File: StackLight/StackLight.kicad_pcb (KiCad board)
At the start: 2 copper layers, 40.6 x 35.5 mm, 3 parts, among them J1 RJ45, J2 Conn_01x05

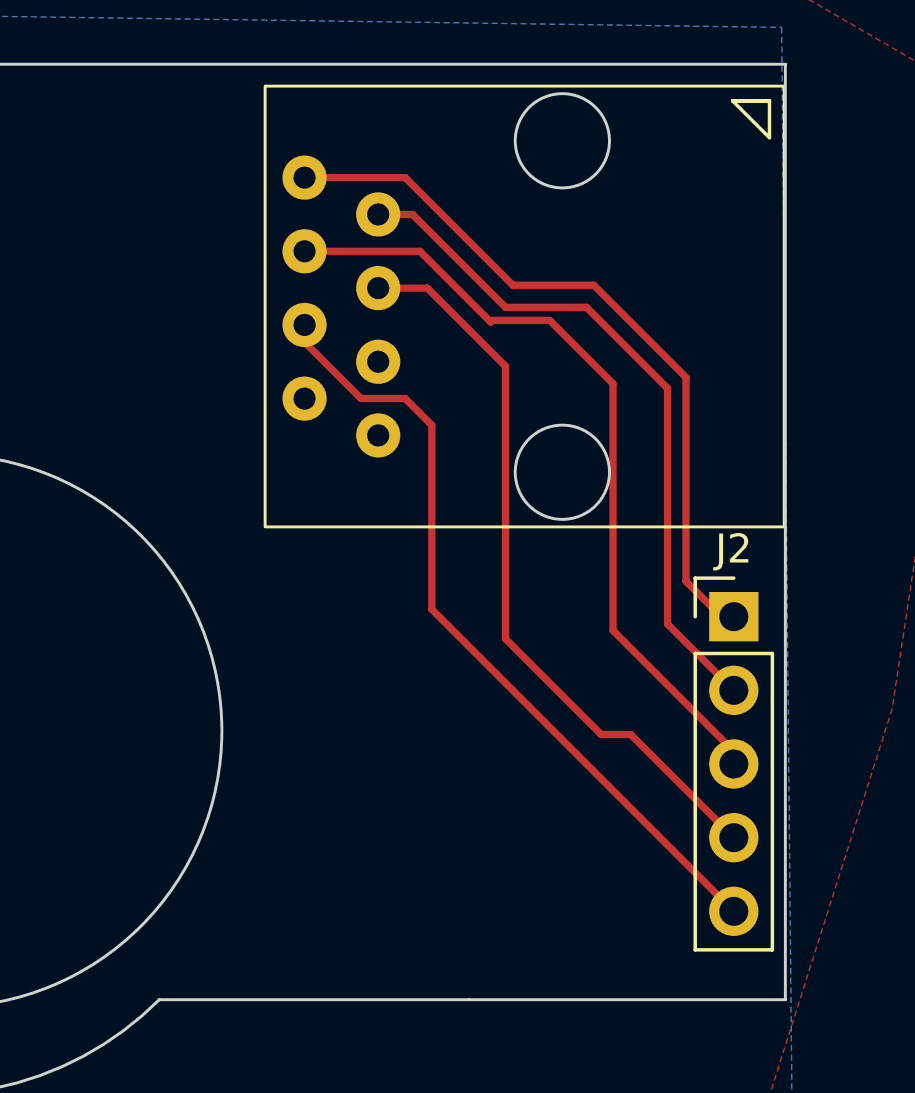
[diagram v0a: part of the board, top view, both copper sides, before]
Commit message: Updated Button and Stacklight PCB to not have backwards fucking footprint shit.
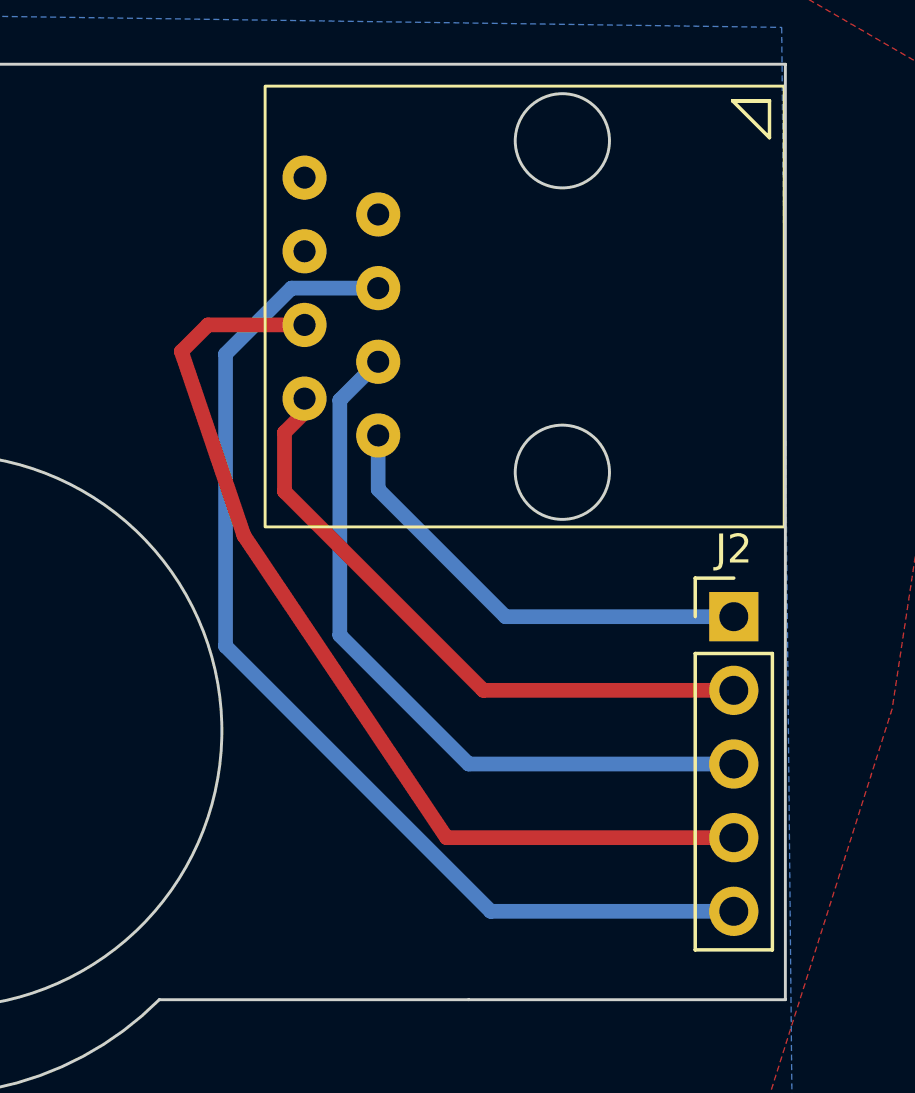
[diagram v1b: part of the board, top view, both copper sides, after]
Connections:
- J1 pad 1: unconnected-(J1-Pad1) -> Net-(J2-Pin_1)
- J1 pad 2: unconnected-(J1-Pad2) -> Net-(J2-Pin_2)
- J1 pad 3: unconnected-(J1-Pad3) -> Net-(J2-Pin_3)
- J1 pad 4: Net-(J1-Pad4) -> Net-(J2-Pin_4)
- J1 pad 5: Net-(J1-Pad5) -> Net-(J2-Pin_5)
- J1 pad 6: Net-(J1-Pad6) -> unconnected-(J1-Pad6)
- J1 pad 7: Net-(J1-Pad7) -> unconnected-(J1-Pad7)
- J1 pad 8: Net-(J1-Pad8) -> unconnected-(J1-Pad8)
- J2 pad 1: Net-(J1-Pad8) -> Net-(J2-Pin_1)
- J2 pad 2: Net-(J1-Pad7) -> Net-(J2-Pin_2)
- J2 pad 3: Net-(J1-Pad6) -> Net-(J2-Pin_3)
- J2 pad 4: Net-(J1-Pad5) -> Net-(J2-Pin_4)
- J2 pad 5: Net-(J1-Pad4) -> Net-(J2-Pin_5)
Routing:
- net Net-(J2-Pin_5): track 0.00 -> 37.6 mm
- net Net-(J2-Pin_4): track 0.00 -> 33.8 mm
- net Net-(J1-Pad6): track 27.4 -> 0.00 mm
- net Net-(J1-Pad4): track 26.6 -> 0.00 mm
- net Net-(J1-Pad5): track 25.6 -> 0.00 mm
- net Net-(J2-Pin_3): track 0.00 -> 25.4 mm
- net Net-(J1-Pad8): track 25.2 -> 0.00 mm
- net Net-(J1-Pad7): track 23.8 -> 0.00 mm
- net Net-(J2-Pin_2): track 0.00 -> 21.8 mm
- net Net-(J2-Pin_1): track 0.00 -> 15.9 mm
- added copper zone on B.Cu, net Net-(J2-Pin_1)
- removed copper zone on B.Cu, net unconnected-(J1-Pad1)
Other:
- board text added: "STACKLIGHT ADAPTER VERSION 3 FOR ARENA CONTROL v4 Kim C."
- board text removed: "stack light adapter v2, 2023 kim c."

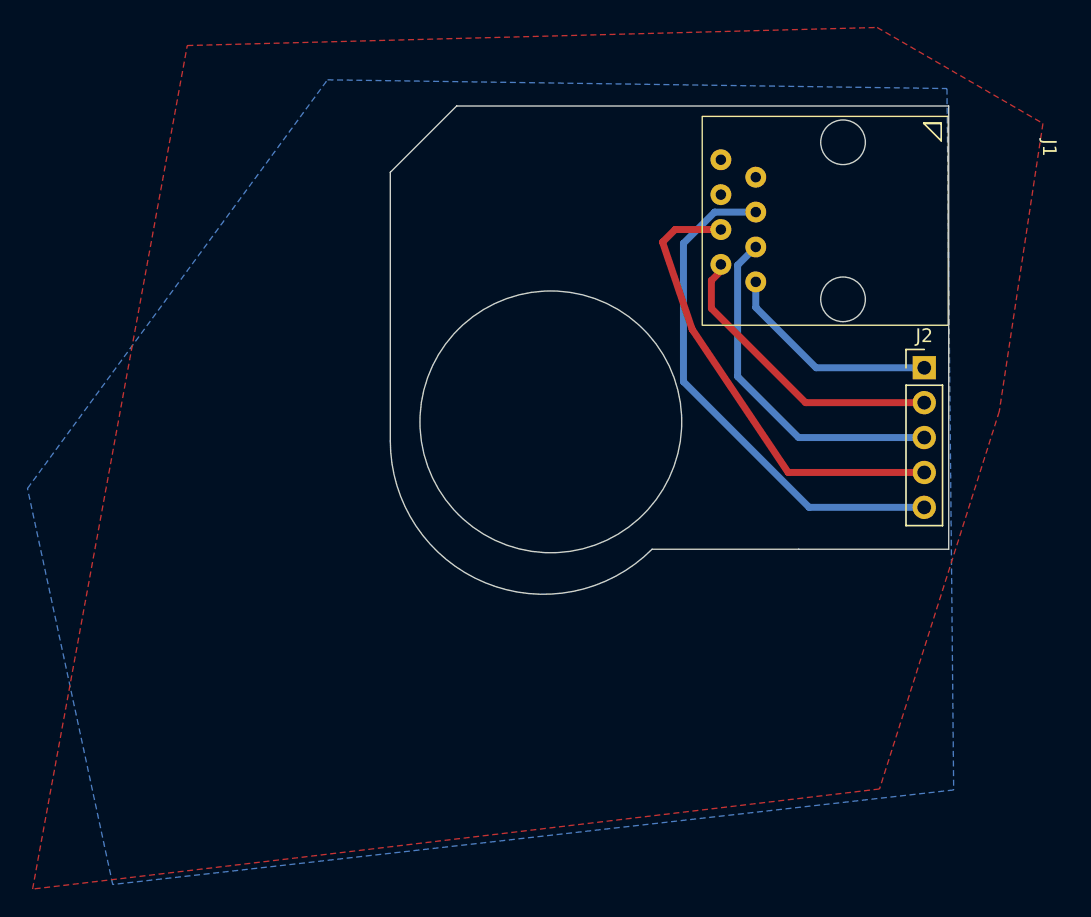
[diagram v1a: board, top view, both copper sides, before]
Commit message: Update to non-hole design.  Verify wire gagues.
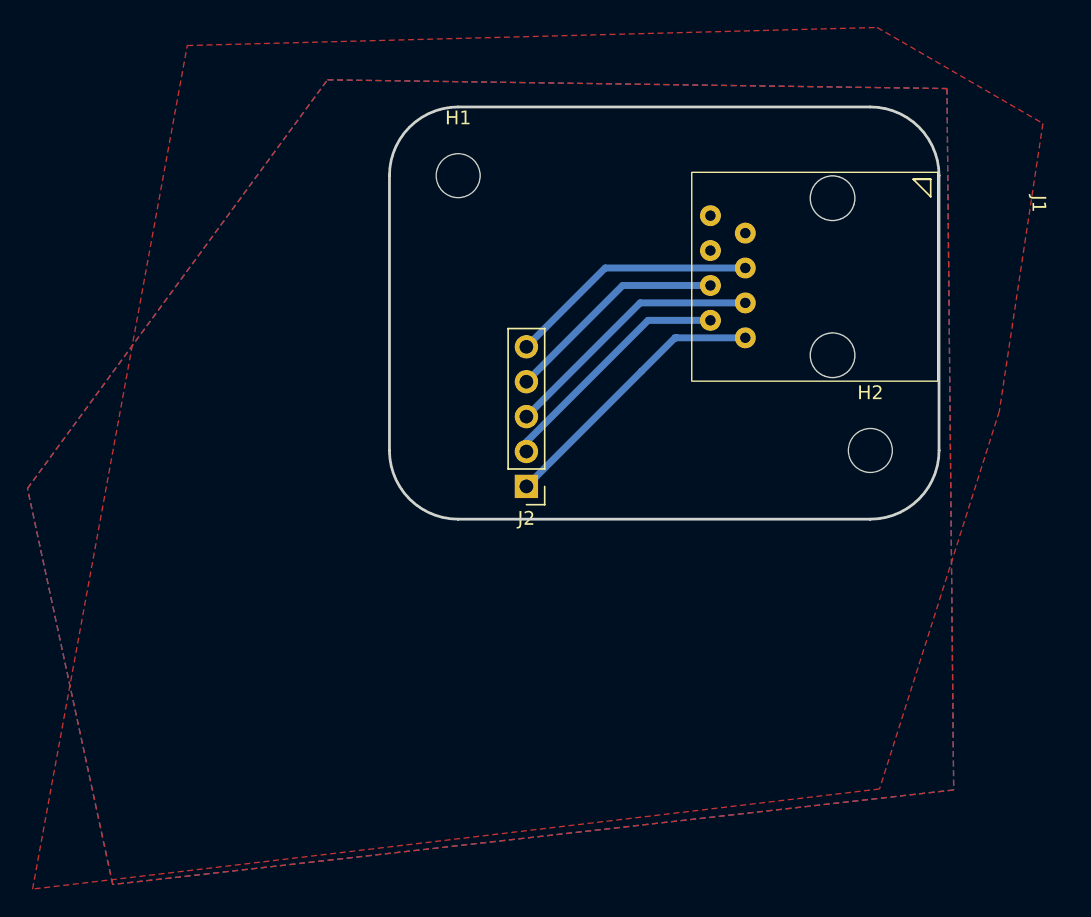
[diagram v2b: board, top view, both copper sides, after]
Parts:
- added H1: MountingHole, MountingHole:MountingHole_3.2mm_M3, F.Cu at (120.0, 80.0)
- added H2: MountingHole, MountingHole:MountingHole_3.2mm_M3, F.Cu at (150.0, 100.0)
- moved J2 30.2 mm to (125.0, 102.6), turned to 180 degrees
- moved kibuzzard-631545B4 4.58 mm to (152.4, 87.6)
- moved J1 4.14 mm to (154.9, 79.8)
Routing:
- net Net-(J2-Pin_5): track 37.6 -> 18.3 mm
- net Net-(J2-Pin_4): track 33.8 -> 16.3 mm
- net Net-(J2-Pin_3): track 25.4 -> 19.4 mm
- net Net-(J2-Pin_1): track 15.9 -> 20.4 mm
- net Net-(J2-Pin_2): track 21.8 -> 17.8 mm
- added copper zone on B.Cu, net (none)
- removed copper zone on B.Cu, net Net-(J2-Pin_1)
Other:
- board size 40.6 x 35.5 mm -> 40 x 30 mm
- board text added: "STACKLIGHT ADAPTER VERSION 3 Kim C."
- board text removed: "STACKLIGHT ADAPTER VERSION 3 FOR ARENA CONTROL v4 Kim C."

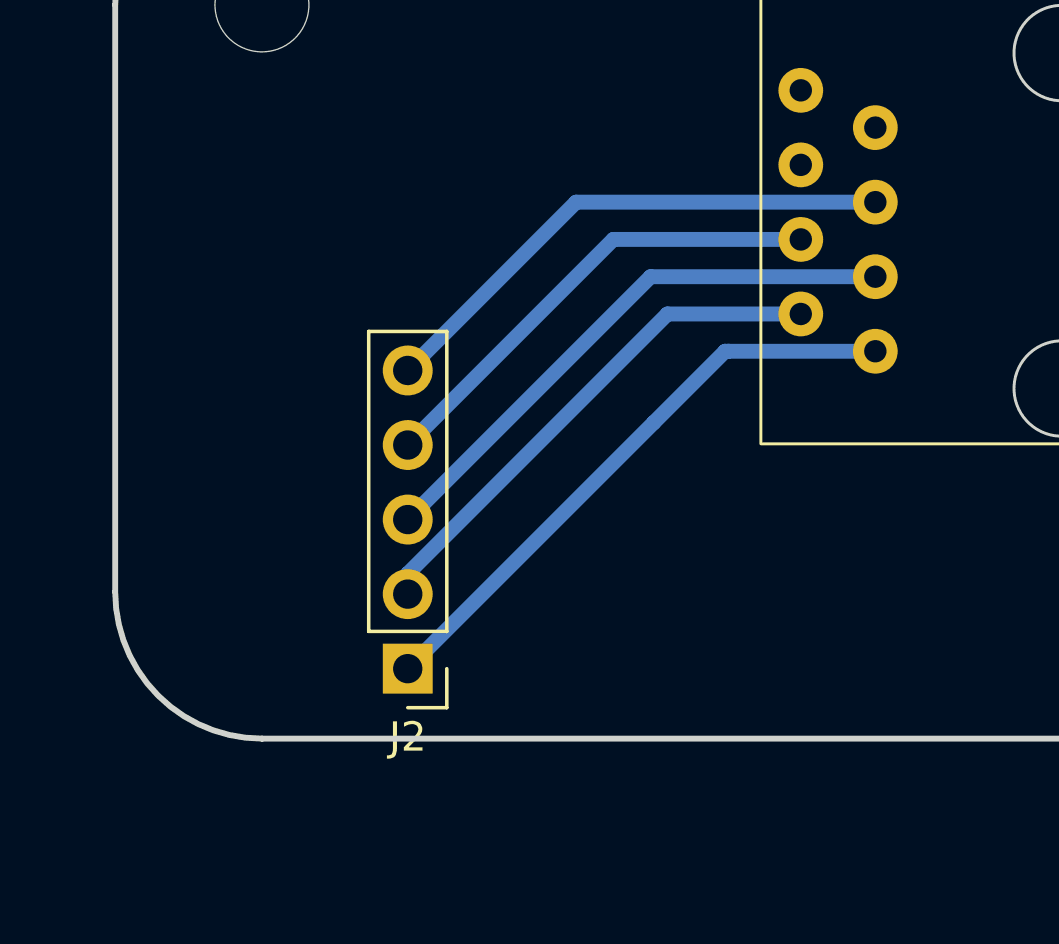
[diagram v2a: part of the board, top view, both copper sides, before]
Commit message: Added wire strain relief that should fit.
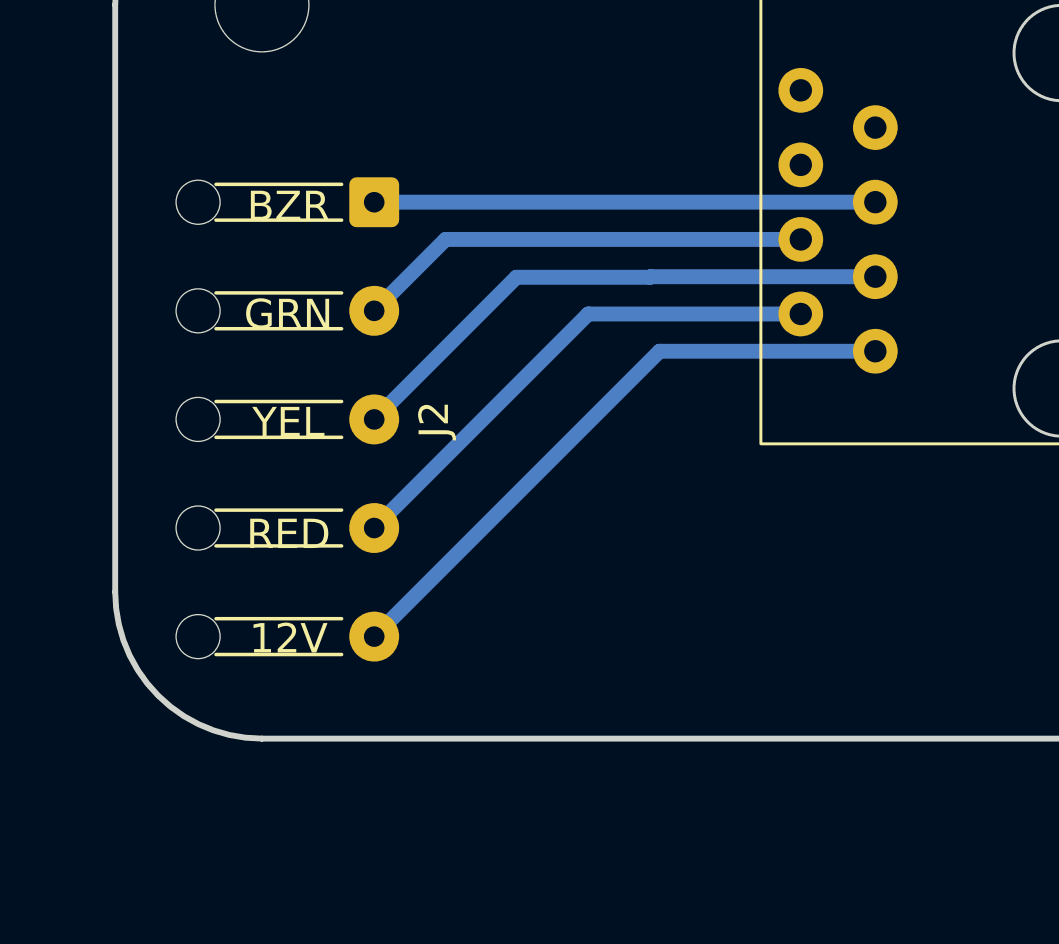
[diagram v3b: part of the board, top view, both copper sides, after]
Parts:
- J2: footprint Connector_PinHeader_2.54mm:PinHeader_1x05_P2.54mm_Vertical -> Connector_Wire:SolderWire-0.127sqmm_1x05_P3.7mm_D0.48mm_OD1mm_Relief
- moved J2 15.9 mm to (123.8, 86.7), turned to -90 degrees
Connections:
- net Net-(J2-Pin_3) renamed /YEL
- J1 pad 1: Net-(J2-Pin_1) -> /12V
- J1 pad 2: Net-(J2-Pin_2) -> /RED
- J1 pad 4: Net-(J2-Pin_4) -> /GRN
- J1 pad 5: Net-(J2-Pin_5) -> /BZR
- J2 pad 1: Net-(J2-Pin_1) -> /BZR
- J2 pad 2: Net-(J2-Pin_2) -> /GRN
- J2 pad 4: Net-(J2-Pin_4) -> /RED
- J2 pad 5: Net-(J2-Pin_5) -> /12V
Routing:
- net /12V: track 0.00 -> 21.1 mm
- net Net-(J2-Pin_1): track 20.4 -> 0.00 mm
- net Net-(J2-Pin_5): track 18.3 -> 0.00 mm
- net Net-(J2-Pin_2): track 17.8 -> 0.00 mm
- net /RED: track 0.00 -> 17.6 mm
- net /BZR: track 0.00 -> 17.1 mm
- net Net-(J2-Pin_4): track 16.3 -> 0.00 mm
- net /GRN: track 0.00 -> 15.5 mm

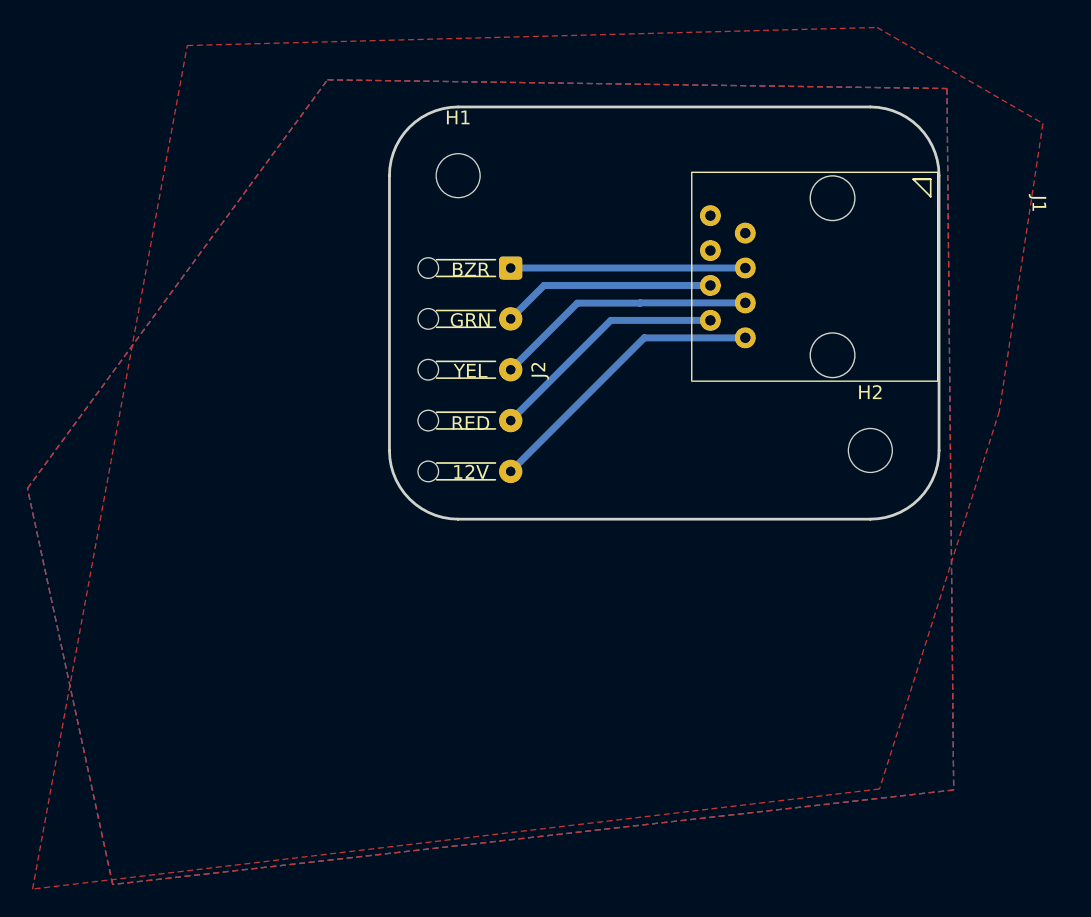
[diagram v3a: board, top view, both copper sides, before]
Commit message: Updated PCB revisions, swapped to larger footprint for stacklight connector, release cutting soon.
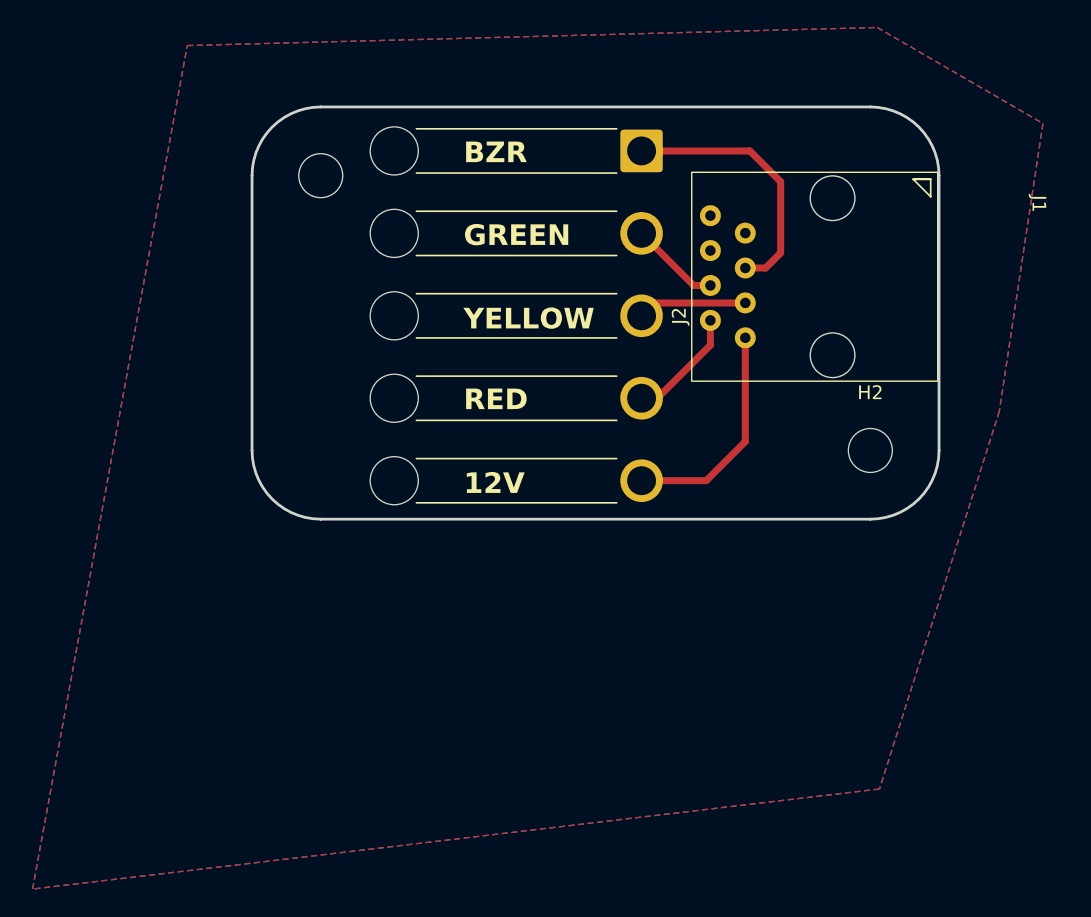
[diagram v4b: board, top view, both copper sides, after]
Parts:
- H1: moved to B.Cu
- J2: footprint Connector_Wire:SolderWire-0.127sqmm_1x05_P3.7mm_D0.48mm_OD1mm_Relief -> Connector_Wire:SolderWire-1.5sqmm_1x05_P6mm_D1.7mm_OD3mm_Relief
- moved J2 12.8 mm to (133.3, 78.2)
- moved H1 10.0 mm to (110.0, 80.0), turned to 180 degrees
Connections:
- J1 pad 8: unconnected-(J1-Pad8) -> GND
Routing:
- net /YEL: track 19.1 -> 7.94 mm
- net /RED: track 17.6 -> 8.42 mm
- net /GRN: track 15.5 -> 6.58 mm
- net /12V: track 21.1 -> 16.3 mm
- net /BZR: track 17.1 -> 19.3 mm
- added copper zone on B.Cu, net GND
- added copper zone on F.Cu, net GND
- removed copper zone on B.Cu, net (none)
- removed copper zone on F.Cu, net (none)
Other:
- board size 40 x 30 mm -> 50 x 30 mm
- board text added: "GREEN"
- board text added: "STACKLIGHT ADAPTER VERSION 4 Kim C."
- board text added: "YELLOW"
- board text removed: "GRN"
- board text removed: "STACKLIGHT ADAPTER VERSION 3 Kim C."
- board text removed: "YEL"

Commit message: Update repo to use consistent gerber outputs; yay!
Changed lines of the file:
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@@
       (drillshape 0)
       (scaleselection 1)
-      (outputdirectory "grb/")
+      (outputdirectory "gerbers/")
     )
   )
@@
     (pad "" np_thru_hole circle (at 18 18 270) (size 3.5 3.5) (drill 3.5) (layers "*.Cu" "*.Mask"))
     (pad "" np_thru_hole circle (at 24 18 270) (size 3.5 3.5) (drill 3.5) (layers "*.Cu" "*.Mask"))
-    (pad "1" thru_hole roundrect (at 0 0 270) (size 3.1 3.1) (drill 2.1) (layers "*.Cu" "*.Mask") (roundrect_rratio 0.080645)
+    (pad "1" thru_hole roundrect (at 0 0 270) (size 3.1 3.1) (drill 2.1) (layers "*.Cu" "*.Mask") (roundrect_rratio 0.08064483871)
       (net 5 "/BZR") (pinfunction "Pin_1") (pintype "passive"))
     (pad "2" thru_hole circle (at 6 0 270) (size 3.1 3.1) (drill 2.1) (layers "*.Cu" "*.Mask")
